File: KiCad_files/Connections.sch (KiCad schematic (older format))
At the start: 4 parts, among them U1 XC7A35T_CSG325

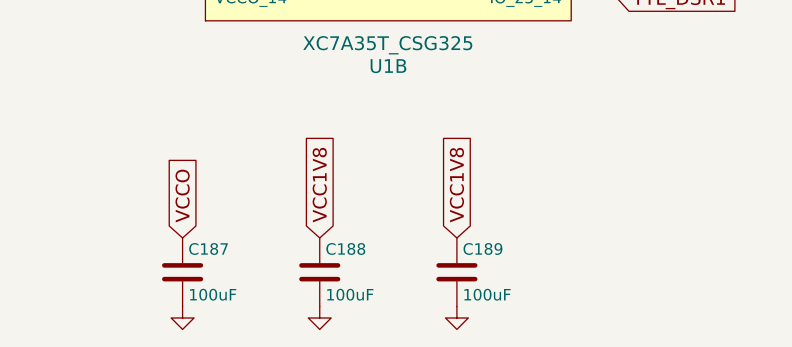
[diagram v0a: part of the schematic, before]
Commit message: Added more caps and jumpers for EMCCLK & Config
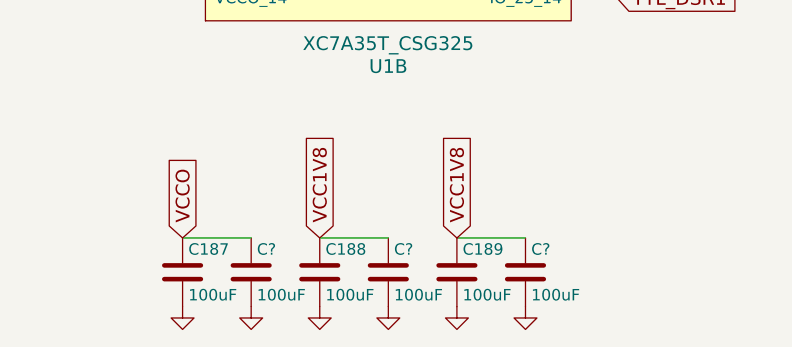
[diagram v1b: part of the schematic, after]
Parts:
- added C? (x3): 100uF, symbol Device:C
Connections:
- net GND: now also C?.2, C?.2, C?.2
- net VCC1V8: now also C?.1, C?.1
- net VCCO: now also C?.1
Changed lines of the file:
@@
 Text GLabel 6500 2300 2    60   Input ~ 0
 I2C_SDA
+$Comp
+L Device:C C?
+U 1 1 5C7929E6
+P 2800 7200
+F 0 "C?" H 2825 7300 50  0000 L CNN
+F 1 "100uF" H 2825 7100 50  0000 L CNN
+F 2 "" H 2838 7050 50  0001 C CNN
+F 3 "" H 2800 7200 50  0001 C CNN
+	1    2800 7200
+	1    0    0    -1
+$EndComp
+$Comp
+L power:GND #PWR?
+U 1 1 5C7929EC
+P 2800 7350
+F 0 "#PWR?" H 2800 7100 50  0001 C CNN
+F 1 "GND" H 2800 7200 50  0001 C CNN
+F 2 "" H 2800 7350 50  0001 C CNN
+F 3 "" H 2800 7350 50  0001 C CNN
+	1    2800 7350
+	1    0    0    -1
+$EndComp
+Wire Wire Line
+	2500 7050 2800 7050
+$Comp
+L Device:C C?
+U 1 1 5C7935EE
+P 2200 7200
+F 0 "C?" H 2225 7300 50  0000 L CNN
+F 1 "100uF" H 2225 7100 50  0000 L CNN
+F 2 "" H 2238 7050 50  0001 C CNN
+F 3 "" H 2200 7200 50  0001 C CNN
+	1    2200 7200
+	1    0    0    -1
+$EndComp
+$Comp
+L power:GND #PWR?
+U 1 1 5C7935F5
+P 2200 7350
+F 0 "#PWR?" H 2200 7100 50  0001 C CNN
+F 1 "GND" H 2200 7200 50  0001 C CNN
+F 2 "" H 2200 7350 50  0001 C CNN
+F 3 "" H 2200 7350 50  0001 C CNN
+	1    2200 7350
+	1    0    0    -1
+$EndComp
+Wire Wire Line
+	1900 7050 2200 7050
+$Comp
+L Device:C C?
+U 1 1 5C793CA4
+P 1600 7200
+F 0 "C?" H 1625 7300 50  0000 L CNN
+F 1 "100uF" H 1625 7100 50  0000 L CNN
+F 2 "" H 1638 7050 50  0001 C CNN
+F 3 "" H 1600 7200 50  0001 C CNN
+	1    1600 7200
+	1    0    0    -1
+$EndComp
+$Comp
+L power:GND #PWR?
+U 1 1 5C793CAB
+P 1600 7350
+F 0 "#PWR?" H 1600 7100 50  0001 C CNN
+F 1 "GND" H 1600 7200 50  0001 C CNN
+F 2 "" H 1600 7350 50  0001 C CNN
+F 3 "" H 1600 7350 50  0001 C CNN
+	1    1600 7350
+	1    0    0    -1
+$EndComp
+Wire Wire Line
+	1300 7050 1600 7050
 $EndSCHEMATC

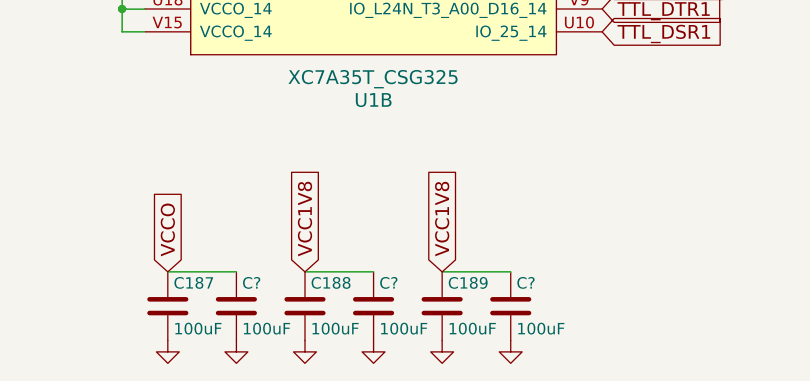
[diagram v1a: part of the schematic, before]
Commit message: Annotations and proper connections
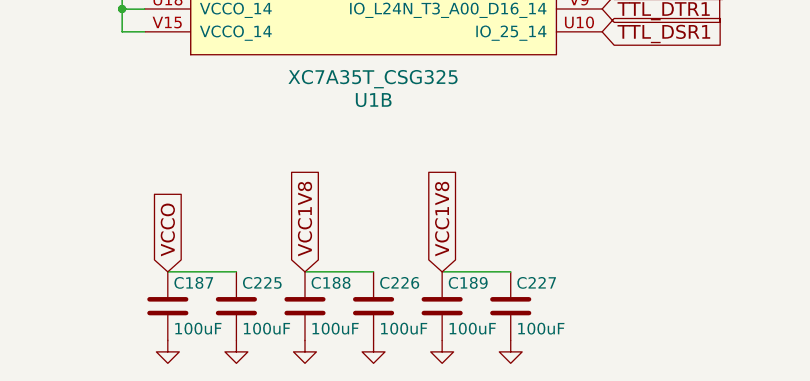
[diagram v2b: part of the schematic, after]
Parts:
- gave numbers to parts that had none: 3
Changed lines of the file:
@@
 I2C_SDA
 $Comp
-L Device:C C?
+L Device:C C227
 U 1 1 5C7929E6
 P 2800 7200
-F 0 "C?" H 2825 7300 50  0000 L CNN
+F 0 "C227" H 2825 7300 50  0000 L CNN
 F 1 "100uF" H 2825 7100 50  0000 L CNN
 F 2 "" H 2838 7050 50  0001 C CNN
@@
 $EndComp
 $Comp
-L power:GND #PWR?
+L power:GND #PWR0141
 U 1 1 5C7929EC
 P 2800 7350
-F 0 "#PWR?" H 2800 7100 50  0001 C CNN
+F 0 "#PWR0141" H 2800 7100 50  0001 C CNN
 F 1 "GND" H 2800 7200 50  0001 C CNN
 F 2 "" H 2800 7350 50  0001 C CNN
@@
 	2500 7050 2800 7050
 $Comp
-L Device:C C?
+L Device:C C226
 U 1 1 5C7935EE
 P 2200 7200
-F 0 "C?" H 2225 7300 50  0000 L CNN
+F 0 "C226" H 2225 7300 50  0000 L CNN
 F 1 "100uF" H 2225 7100 50  0000 L CNN
 F 2 "" H 2238 7050 50  0001 C CNN
@@
 $EndComp
 $Comp
-L power:GND #PWR?
+L power:GND #PWR0140
 U 1 1 5C7935F5
 P 2200 7350
-F 0 "#PWR?" H 2200 7100 50  0001 C CNN
+F 0 "#PWR0140" H 2200 7100 50  0001 C CNN
 F 1 "GND" H 2200 7200 50  0001 C CNN
 F 2 "" H 2200 7350 50  0001 C CNN
@@
 	1900 7050 2200 7050
 $Comp
-L Device:C C?
+L Device:C C225
 U 1 1 5C793CA4
 P 1600 7200
-F 0 "C?" H 1625 7300 50  0000 L CNN
+F 0 "C225" H 1625 7300 50  0000 L CNN
 F 1 "100uF" H 1625 7100 50  0000 L CNN
 F 2 "" H 1638 7050 50  0001 C CNN
@@
 $EndComp
 $Comp
-L power:GND #PWR?
+L power:GND #PWR0139
 U 1 1 5C793CAB
 P 1600 7350
-F 0 "#PWR?" H 1600 7100 50  0001 C CNN
+F 0 "#PWR0139" H 1600 7100 50  0001 C CNN
 F 1 "GND" H 1600 7200 50  0001 C CNN
 F 2 "" H 1600 7350 50  0001 C CNN
